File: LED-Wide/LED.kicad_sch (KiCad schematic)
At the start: 4 parts, among them J1 Conn_01x02_Pin, J2 Conn_01x02_Pin

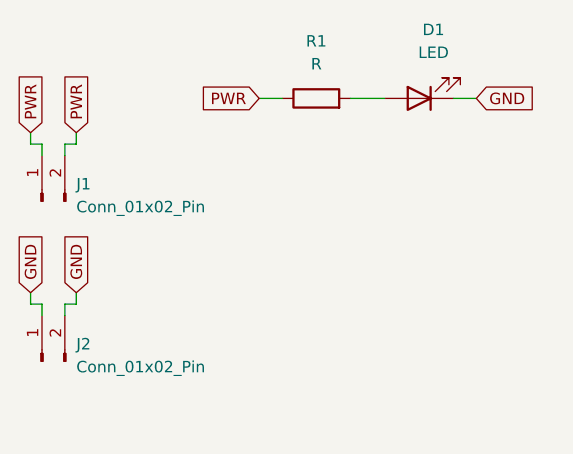
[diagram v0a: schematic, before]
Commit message: Redesigned LED-Wide PCB; created Fabrication files; added template for fabrication order request; added final order contents.
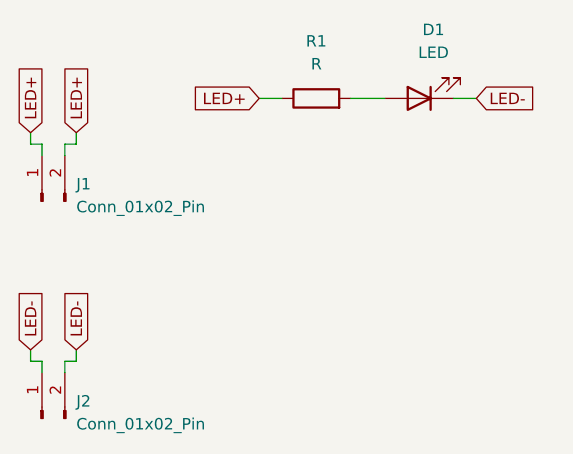
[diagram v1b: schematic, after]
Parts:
- D1: footprint LED_THT:LED_D1.8mm_W3.3mm_H2.4mm -> LED_THT:LED_D5.0mm
- J1, J2: footprint Connector_PinHeader_1.00mm:PinHeader_1x02_P1.00mm_Vertical -> Connector_PinHeader_2.54mm:PinHeader_1x02_P2.54mm_Vertical
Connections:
- net GND renamed LED-
- net PWR renamed LED+
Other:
- moved on the sheet: J2
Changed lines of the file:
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@@
 	(wire
 		(pts
-			(xy 107.95 105.41) (xy 107.95 106.68)
+			(xy 107.95 111.76) (xy 107.95 113.03)
 		)
 		(stroke
@@
 	(wire
 		(pts
-			(xy 111.76 106.68) (xy 111.76 107.95)
-		)
-		(stroke
-			(width 0)
-			(type default)
-		)
-	)
-	(wire
-		(pts
-			(xy 109.22 106.68) (xy 109.22 107.95)
+			(xy 111.76 113.03) (xy 111.76 114.3)
+		)
+		(stroke
+			(width 0)
+			(type default)
+		)
+	)
+	(wire
+		(pts
+			(xy 109.22 113.03) (xy 109.22 114.3)
 		)
 		(stroke
@@
 	(wire
 		(pts
-			(xy 107.95 106.68) (xy 109.22 106.68)
-		)
-		(stroke
-			(width 0)
-			(type default)
-		)
-	)
-	(wire
-		(pts
-			(xy 113.03 105.41) (xy 113.03 106.68)
+			(xy 107.95 113.03) (xy 109.22 113.03)
+		)
+		(stroke
+			(width 0)
+			(type default)
+		)
+	)
+	(wire
+		(pts
+			(xy 113.03 111.76) (xy 113.03 113.03)
 		)
 		(stroke
@@
 	(wire
 		(pts
-			(xy 113.03 106.68) (xy 111.76 106.68)
+			(xy 113.03 113.03) (xy 111.76 113.03)
 		)
 		(stroke
@@
 		)
 	)
-	(global_label "PWR"
+	(global_label "LED+"
 		(shape input)
 		(at 133.35 83.82 180)
@@
 		)
 		(property "Intersheetrefs" "${INTERSHEET_REFS}"
-			(at 126.3734 83.82 0)
+			(at 125.3453 83.82 0)
 			(effects
 				(font
@@
 		)
 	)
-	(global_label "GND"
+	(global_label "LED-"
 		(shape input)
-		(at 113.03 105.41 90)
+		(at 113.03 111.76 90)
 		(fields_autoplaced yes)
 		(effects
@@
 		)
 		(property "Intersheetrefs" "${INTERSHEET_REFS}"
-			(at 113.03 98.5543 90)
+			(at 113.03 103.7553 90)
 			(effects
 				(font
@@
 		)
 	)
-	(global_label "PWR"
+	(global_label "LED+"
 		(shape input)
 		(at 107.95 87.63 90)
@@
 		)
 		(property "Intersheetrefs" "${INTERSHEET_REFS}"
-			(at 107.95 80.6534 90)
+			(at 107.95 79.6253 90)
 			(effects
 				(font
@@
 		)
 	)
-	(global_label "GND"
+	(global_label "LED-"
 		(shape input)
-		(at 107.95 105.41 90)
+		(at 107.95 111.76 90)
 		(fields_autoplaced yes)
 		(effects
@@
 		)
 		(property "Intersheetrefs" "${INTERSHEET_REFS}"
-			(at 107.95 98.5543 90)
+			(at 107.95 103.7553 90)
 			(effects
 				(font
@@
 		)
 	)
-	(global_label "PWR"
+	(global_label "LED+"
 		(shape input)
 		(at 113.03 87.63 90)
@@
 		)
 		(property "Intersheetrefs" "${INTERSHEET_REFS}"
-			(at 113.03 80.6534 90)
+			(at 113.03 79.6253 90)
 			(effects
 				(font
@@
 		)
 	)
-	(global_label "GND"
+	(global_label "LED-"
 		(shape input)
 		(at 157.48 83.82 0)
@@
 		)
 		(property "Intersheetrefs" "${INTERSHEET_REFS}"
-			(at 164.3357 83.82 0)
+			(at 165.4847 83.82 0)
 			(effects
 				(font
@@
 			)
 		)
-		(property "Footprint" "LED_THT:LED_D1.8mm_W3.3mm_H2.4mm"
+		(property "Footprint" "LED_THT:LED_D5.0mm"
 			(at 151.13 83.82 0)
 			(effects
@@
 			)
 		)
-		(property "Footprint" "Connector_PinHeader_1.00mm:PinHeader_1x02_P1.00mm_Vertical"
+		(property "Footprint" "Connector_PinHeader_2.54mm:PinHeader_1x02_P2.54mm_Vertical"
 			(at 109.22 95.25 0)
 			(effects
@@
 	(symbol
 		(lib_id "Connector:Conn_01x02_Pin")
-		(at 109.22 113.03 90)
+		(at 109.22 119.38 90)
 		(unit 1)
 		(exclude_from_sim no)
@@
 		(fields_autoplaced yes)
 		(property "Reference" "J2"
-			(at 113.03 111.1249 90)
+			(at 113.03 117.4749 90)
 			(effects
 				(font
@@
 		)
 		(property "Value" "Conn_01x02_Pin"
-			(at 113.03 113.6649 90)
+			(at 113.03 120.0149 90)
 			(effects
 				(font
@@
 			)
 		)
-		(property "Footprint" "Connector_PinHeader_1.00mm:PinHeader_1x02_P1.00mm_Vertical"
-			(at 109.22 113.03 0)
+		(property "Footprint" "Connector_PinHeader_2.54mm:PinHeader_1x02_P2.54mm_Vertical"
+			(at 109.22 119.38 0)
 			(effects
 				(font
@@
 		)
 		(property "Datasheet" "~"
-			(at 109.22 113.03 0)
+			(at 109.22 119.38 0)
 			(effects
 				(font
@@
 		)
 		(property "Description" "Generic connector, single row, 01x02, script generated"
-			(at 109.22 113.03 0)
-			(effects
-				(font
+			(at 109.22 119.38 0)
+			(effects
+				(font
